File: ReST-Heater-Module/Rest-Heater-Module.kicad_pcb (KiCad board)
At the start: 2 copper layers, 24.5 x 29.5 mm, 17 parts

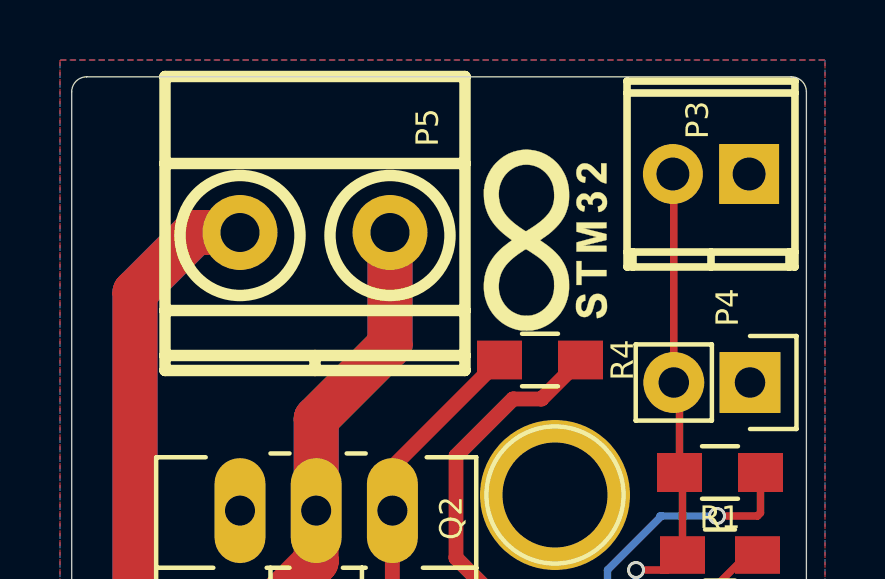
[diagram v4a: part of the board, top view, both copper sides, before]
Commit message: Added IRLML2502 Module and added Ground vias everywhere
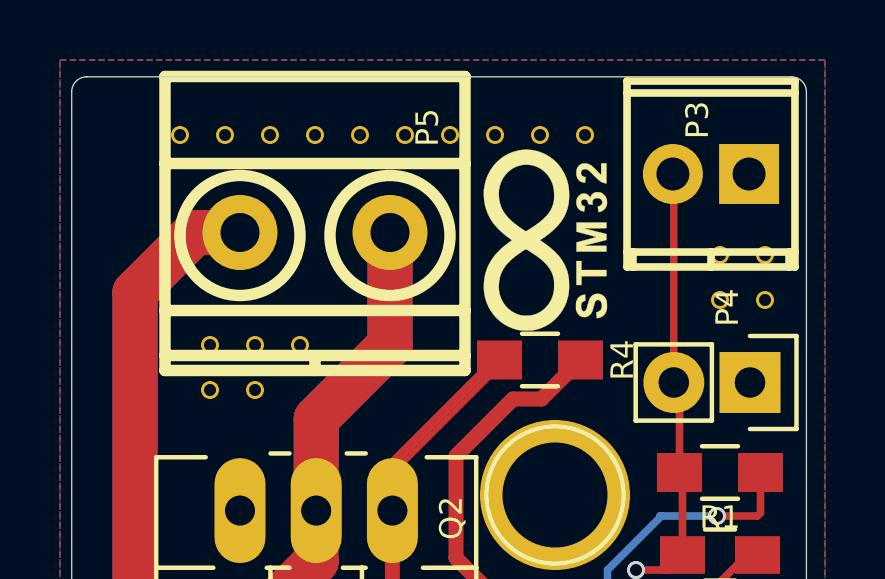
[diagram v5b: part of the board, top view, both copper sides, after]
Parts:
- added 1101: , ReST-Library:VIA-0.6mm, F.Cu at (150.0, 107.0)
- added 111: , ReST-Library:VIA-0.6mm, F.Cu at (136.5, 107.0)
- added 1111: , ReST-Library:VIA-0.6mm, F.Cu at (137.5, 114.0)
- added 111111: , ReST-Library:VIA-0.6mm, F.Cu at (154.5, 111.0)
- added 111112: , ReST-Library:VIA-0.6mm, F.Cu at (154.5, 112.5)
- added 111121: , ReST-Library:VIA-0.6mm, F.Cu at (156.0, 111.0)
- added 111122: , ReST-Library:VIA-0.6mm, F.Cu at (156.0, 112.5)
- added 1112: , ReST-Library:VIA-0.6mm, F.Cu at (137.5, 115.5)
- added 1121: , ReST-Library:VIA-0.6mm, F.Cu at (139.0, 114.0)
- added 1122: , ReST-Library:VIA-0.6mm, F.Cu at (139.0, 115.5)
- added 1131: , ReST-Library:VIA-0.6mm, F.Cu at (140.5, 114.0)
- added 121: , ReST-Library:VIA-0.6mm, F.Cu at (138.0, 107.0)
- added 131: , ReST-Library:VIA-0.6mm, F.Cu at (139.5, 107.0)
- added 141: , ReST-Library:VIA-0.6mm, F.Cu at (141.0, 107.0)
- added 151: , ReST-Library:VIA-0.6mm, F.Cu at (142.5, 107.0)
- added 161: , ReST-Library:VIA-0.6mm, F.Cu at (144.0, 107.0)
- added 171: , ReST-Library:VIA-0.6mm, F.Cu at (145.5, 107.0)
- added 181: , ReST-Library:VIA-0.6mm, F.Cu at (147.0, 107.0)
- added 191: , ReST-Library:VIA-0.6mm, F.Cu at (148.5, 107.0)
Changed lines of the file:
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@@
 (kicad_pcb (version 4) (host pcbnew 4.0.1-stable)
   (general
-    (links 34)
+    (links 50)
     (no_connects 0)
-    (area 132.5 104.5 159.575 143.485001)
+    (area 132.884999 105.054999 157.385001 134.605001)
     (thickness 1.6)
     (drawings 9)
     (tracks 116)
     (zones 0)
-    (modules 17)
+    (modules 36)
     (nets 11)
   )
@@
     (mod_text_size 1 1)
     (mod_text_width 0.15)
-    (pad_size 5 5)
-    (pad_drill 3.5)
+    (pad_size 0.6 0.6)
+    (pad_drill 0.4)
     (pad_to_mask_clearance 0)
     (aux_axis_origin 0 0)
@@
     (add_net "Net-(D2-Pad2)")
     (add_net "Net-(Q1-Pad3)")
+  )
+  (module ReST-Library:VIA-0.6mm (layer F.Cu)
+    (at 156 112.5)
+    (fp_text reference 111122 (at 0 3.5) (layer F.SilkS) hide
+      (effects (font (size 1 1) (thickness 0.15)))
+    )
+    (fp_text value "" (at 0 -3) (layer F.Fab) hide
+      (effects (font (size 1 1) (thickness 0.15)))
+    )
+    (pad 1 thru_hole circle (at 0 0) (size 0.6 0.6) (drill 0.4) (layers *.Cu)
+      (net 2 GND) (zone_connect 2))
+  )
+  (module ReST-Library:VIA-0.6mm (layer F.Cu)
+    (at 154.5 112.5)
+    (fp_text reference 111112 (at 0 3.5) (layer F.SilkS) hide
+      (effects (font (size 1 1) (thickness 0.15)))
+    )
+    (fp_text value "" (at 0 -3) (layer F.Fab) hide
+      (effects (font (size 1 1) (thickness 0.15)))
+    )
+    (pad 1 thru_hole circle (at 0 0) (size 0.6 0.6) (drill 0.4) (layers *.Cu)
+      (net 2 GND) (zone_connect 2))
+  )
+  (module ReST-Library:VIA-0.6mm (layer F.Cu)
+    (at 156 111)
+    (fp_text reference 111121 (at 0 3.5) (layer F.SilkS) hide
+      (effects (font (size 1 1) (thickness 0.15)))
+    )
+    (fp_text value "" (at 0 -3) (layer F.Fab) hide
+      (effects (font (size 1 1) (thickness 0.15)))
+    )
+    (pad 1 thru_hole circle (at 0 0) (size 0.6 0.6) (drill 0.4) (layers *.Cu)
+      (net 2 GND) (zone_connect 2))
+  )
+  (module ReST-Library:VIA-0.6mm (layer F.Cu)
+    (at 154.5 111)
+    (fp_text reference 111111 (at 0 3.5) (layer F.SilkS) hide
+      (effects (font (size 1 1) (thickness 0.15)))
+    )
+    (fp_text value "" (at 0 -3) (layer F.Fab) hide
+      (effects (font (size 1 1) (thickness 0.15)))
+    )
+    (pad 1 thru_hole circle (at 0 0) (size 0.6 0.6) (drill 0.4) (layers *.Cu)
+      (net 2 GND) (zone_connect 2))
+  )
+  (module ReST-Library:VIA-0.6mm (layer F.Cu)
+    (at 139 115.5)
+    (fp_text reference 1122 (at 0 3.5) (layer F.SilkS) hide
+      (effects (font (size 1 1) (thickness 0.15)))
+    )
+    (fp_text value "" (at 0 -3) (layer F.Fab) hide
+      (effects (font (size 1 1) (thickness 0.15)))
+    )
+    (pad 1 thru_hole circle (at 0 0) (size 0.6 0.6) (drill 0.4) (layers *.Cu)
+      (net 2 GND) (zone_connect 2))
+  )
+  (module ReST-Library:VIA-0.6mm (layer F.Cu)
+    (at 137.5 115.5)
+    (fp_text reference 1112 (at 0 3.5) (layer F.SilkS) hide
+      (effects (font (size 1 1) (thickness 0.15)))
+    )
+    (fp_text value "" (at 0 -3) (layer F.Fab) hide
+      (effects (font (size 1 1) (thickness 0.15)))
+    )
+    (pad 1 thru_hole circle (at 0 0) (size 0.6 0.6) (drill 0.4) (layers *.Cu)
+      (net 2 GND) (zone_connect 2))
+  )
+  (module ReST-Library:VIA-0.6mm (layer F.Cu)
+    (at 140.5 114)
+    (fp_text reference 1131 (at 0 3.5) (layer F.SilkS) hide
+      (effects (font (size 1 1) (thickness 0.15)))
+    )
+    (fp_text value "" (at 0 -3) (layer F.Fab) hide
+      (effects (font (size 1 1) (thickness 0.15)))
+    )
+    (pad 1 thru_hole circle (at 0 0) (size 0.6 0.6) (drill 0.4) (layers *.Cu)
+      (net 2 GND) (zone_connect 2))
+  )
+  (module ReST-Library:VIA-0.6mm (layer F.Cu)
+    (at 139 114)
+    (fp_text reference 1121 (at 0 3.5) (layer F.SilkS) hide
+      (effects (font (size 1 1) (thickness 0.15)))
+    )
+    (fp_text value "" (at 0 -3) (layer F.Fab) hide
+      (effects (font (size 1 1) (thickness 0.15)))
+    )
+    (pad 1 thru_hole circle (at 0 0) (size 0.6 0.6) (drill 0.4) (layers *.Cu)
+      (net 2 GND) (zone_connect 2))
+  )
+  (module ReST-Library:VIA-0.6mm (layer F.Cu)
+    (at 137.5 114)
+    (fp_text reference 1111 (at 0 3.5) (layer F.SilkS) hide
+      (effects (font (size 1 1) (thickness 0.15)))
+    )
+    (fp_text value "" (at 0 -3) (layer F.Fab) hide
+      (effects (font (size 1 1) (thickness 0.15)))
+    )
+    (pad 1 thru_hole circle (at 0 0) (size 0.6 0.6) (drill 0.4) (layers *.Cu)
+      (net 2 GND) (zone_connect 2))
+  )
+  (module ReST-Library:VIA-0.6mm (layer F.Cu)
+    (at 150 107)
+    (fp_text reference 1101 (at 0 3.5) (layer F.SilkS) hide
+      (effects (font (size 1 1) (thickness 0.15)))
+    )
+    (fp_text value "" (at 0 -3) (layer F.Fab) hide
+      (effects (font (size 1 1) (thickness 0.15)))
+    )
+    (pad 1 thru_hole circle (at 0 0) (size 0.6 0.6) (drill 0.4) (layers *.Cu)
+      (net 2 GND) (zone_connect 2))
+  )
+  (module ReST-Library:VIA-0.6mm (layer F.Cu)
+    (at 148.5 107)
+    (fp_text reference 191 (at 0 3.5) (layer F.SilkS) hide
+      (effects (font (size 1 1) (thickness 0.15)))
+    )
+    (fp_text value "" (at 0 -3) (layer F.Fab) hide
+      (effects (font (size 1 1) (thickness 0.15)))
+    )
+    (pad 1 thru_hole circle (at 0 0) (size 0.6 0.6) (drill 0.4) (layers *.Cu)
+      (net 2 GND) (zone_connect 2))
+  )
+  (module ReST-Library:VIA-0.6mm (layer F.Cu)
+    (at 147 107)
+    (fp_text reference 181 (at 0 3.5) (layer F.SilkS) hide
+      (effects (font (size 1 1) (thickness 0.15)))
+    )
+    (fp_text value "" (at 0 -3) (layer F.Fab) hide
+      (effects (font (size 1 1) (thickness 0.15)))
+    )
+    (pad 1 thru_hole circle (at 0 0) (size 0.6 0.6) (drill 0.4) (layers *.Cu)
+      (net 2 GND) (zone_connect 2))
+  )
+  (module ReST-Library:VIA-0.6mm (layer F.Cu)
+    (at 145.5 107)
+    (fp_text reference 171 (at 0 3.5) (layer F.SilkS) hide
+      (effects (font (size 1 1) (thickness 0.15)))
+    )
+    (fp_text value "" (at 0 -3) (layer F.Fab) hide
+      (effects (font (size 1 1) (thickness 0.15)))
+    )
+    (pad 1 thru_hole circle (at 0 0) (size 0.6 0.6) (drill 0.4) (layers *.Cu)
+      (net 2 GND) (zone_connect 2))
+  )
+  (module ReST-Library:VIA-0.6mm (layer F.Cu)
+    (at 144 107)
+    (fp_text reference 161 (at 0 3.5) (layer F.SilkS) hide
+      (effects (font (size 1 1) (thickness 0.15)))
+    )
+    (fp_text value "" (at 0 -3) (layer F.Fab) hide
+      (effects (font (size 1 1) (thickness 0.15)))
+    )
+    (pad 1 thru_hole circle (at 0 0) (size 0.6 0.6) (drill 0.4) (layers *.Cu)
+      (net 2 GND) (zone_connect 2))
+  )
+  (module ReST-Library:VIA-0.6mm (layer F.Cu)
+    (at 142.5 107)
+    (fp_text reference 151 (at 0 3.5) (layer F.SilkS) hide
+      (effects (font (size 1 1) (thickness 0.15)))
+    )
+    (fp_text value "" (at 0 -3) (layer F.Fab) hide
+      (effects (font (size 1 1) (thickness 0.15)))
+    )
+    (pad 1 thru_hole circle (at 0 0) (size 0.6 0.6) (drill 0.4) (layers *.Cu)
+      (net 2 GND) (zone_connect 2))
+  )
+  (module ReST-Library:VIA-0.6mm (layer F.Cu)
+    (at 141 107)
+    (fp_text reference 141 (at 0 3.5) (layer F.SilkS) hide
+      (effects (font (size 1 1) (thickness 0.15)))
+    )
+    (fp_text value "" (at 0 -3) (layer F.Fab) hide
+      (effects (font (size 1 1) (thickness 0.15)))
+    )
+    (pad 1 thru_hole circle (at 0 0) (size 0.6 0.6) (drill 0.4) (layers *.Cu)
+      (net 2 GND) (zone_connect 2))
+  )
+  (module ReST-Library:VIA-0.6mm (layer F.Cu)
+    (at 139.5 107)
+    (fp_text reference 131 (at 0 3.5) (layer F.SilkS) hide
+      (effects (font (size 1 1) (thickness 0.15)))
+    )
+    (fp_text value "" (at 0 -3) (layer F.Fab) hide
+      (effects (font (size 1 1) (thickness 0.15)))
+    )
+    (pad 1 thru_hole circle (at 0 0) (size 0.6 0.6) (drill 0.4) (layers *.Cu)
+      (net 2 GND) (zone_connect 2))
+  )
+  (module ReST-Library:VIA-0.6mm (layer F.Cu)
+    (at 138 107)
+    (fp_text reference 121 (at 0 3.5) (layer F.SilkS) hide
+      (effects (font (size 1 1) (thickness 0.15)))
+    )
+    (fp_text value "" (at 0 -3) (layer F.Fab) hide
+      (effects (font (size 1 1) (thickness 0.15)))
+    )
+    (pad 1 thru_hole circle (at 0 0) (size 0.6 0.6) (drill 0.4) (layers *.Cu)
+      (net 2 GND) (zone_connect 2))
   )
   (module Capacitors_SMD:C_0805_HandSoldering (layer F.Cu)
@@
     )
   )
+  (module ReST-Library:VIA-0.6mm (layer F.Cu)
+    (at 136.5 107)
+    (fp_text reference 111 (at 0 3.5) (layer F.SilkS) hide
+      (effects (font (size 1 1) (thickness 0.15)))
+    )
+    (fp_text value "" (at 0 -3) (layer F.Fab) hide
+      (effects (font (size 1 1) (thickness 0.15)))
+    )
+    (pad 1 thru_hole circle (at 0 0) (size 0.6 0.6) (drill 0.4) (layers *.Cu)
+      (net 2 GND) (zone_connect 2))
+  )
   (gr_arc (start 133.39 134.1) (end 133.39 134.6) (angle 90) (layer Edge.Cuts) (width 0.01))

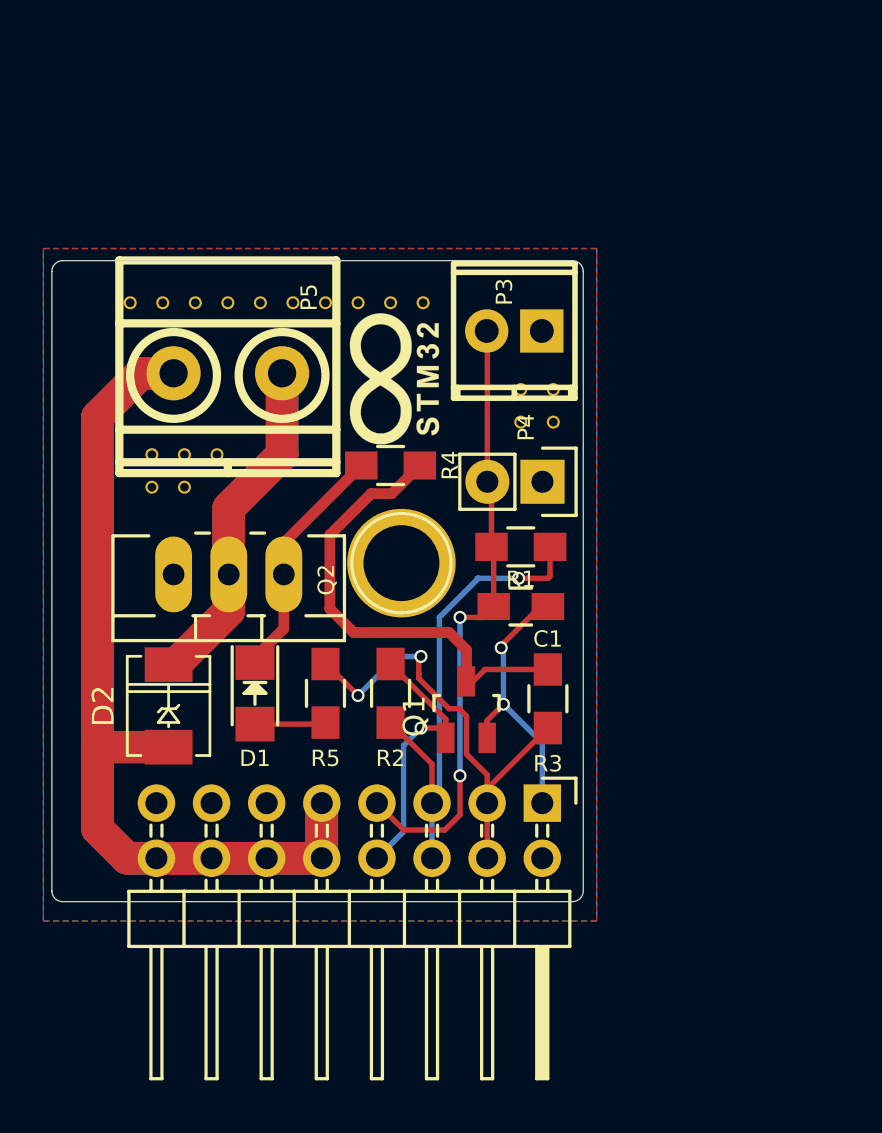
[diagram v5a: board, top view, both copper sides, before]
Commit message: Finished PCB design, notations and silkscreen
gonna work to finish a combined design for cheaper pcb cost and put
everything i need into the bom
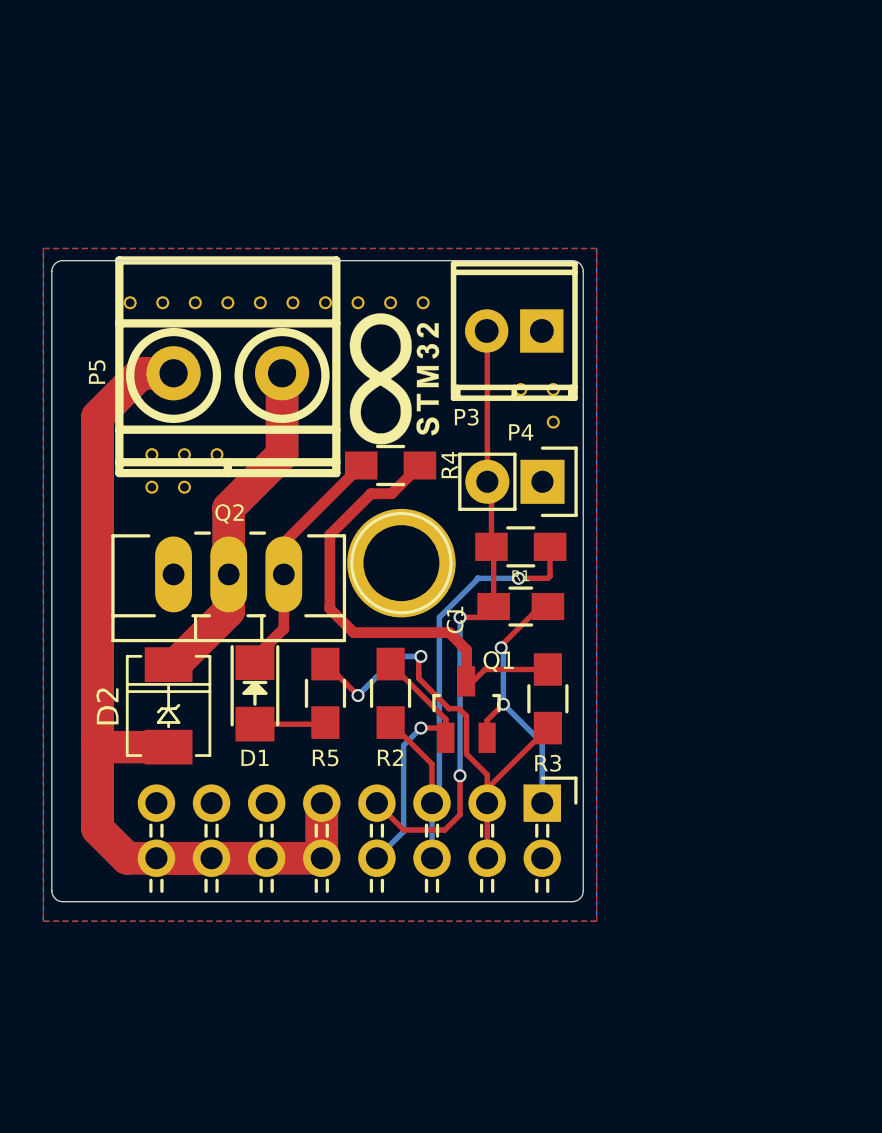
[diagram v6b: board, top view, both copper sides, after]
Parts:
- removed 111112: , ReST-Library:VIA-0.6mm
- ? (x2): renamed from G***; value LOGO -> (none)
- ?: value 1pin -> (none)
- P1: footprint Pin_Headers:Pin_Header_Angled_2x08 -> ReST-Library:Pin_Header_Angled_2x08
- moved ? 0.30 mm to (148.4, 112.7)
- renumbered 111122 to ?, 191 to ?, 181 to ?, 171 to ?, 161 to ?, 151 to ?, 141 to ?, 131 to ?, 121 to ?, 111121 to ?, 111 to ?, 111111 to ?, 1122 to ?, 1112 to ?, 1131 to ?, 1121 to ?, 1111 to ?, 1101 to ?
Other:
- board text added: "ReST32 Heater Rev. A | Test @maker_berry"
- board text removed: "ReST32 Heater Rev. A | Test PCB by Straw"

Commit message: Final release
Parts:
- moved P5 0.30 mm to (141.0, 110.5)
- moved P3 0.08 mm to (154.2, 108.4)
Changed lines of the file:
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@@
     (links 52)
     (no_connects 0)
-    (area 132.5 102.875 159.575 143.485001)
+    (area 132.5 102.875 159.575 135.500001)
     (thickness 1.6)
     (drawings 9)
@@
     (visible_elements 7FFFFFFF)
     (pcbplotparams
-      (layerselection 0x00030_80000001)
-      (usegerberextensions false)
+      (layerselection 0x010f0_80000001)
+      (usegerberextensions true)
       (excludeedgelayer true)
       (linewidth 0.100000)
@@
       (psa4output false)
       (plotreference true)
-      (plotvalue true)
+      (plotvalue false)
       (plotinvisibletext false)
       (padsonsilk false)
@@
       (outputformat 1)
       (mirror false)
-      (drillshape 1)
+      (drillshape 0)
       (scaleselection 1)
-      (outputdirectory ""))
+      (outputdirectory ../Gerber/Heater/))
   )
   (net 0 "")
@@
   )
   (module ReST-Library:screw-2,54-2P (layer F.Cu)
-    (at 154.2 108.3)
+    (at 154.175 108.375)
     (descr "2-way 2.54mm pitch terminal block, Phoenix MPT series")
     (fp_text reference P3 (at -2.2 4 180) (layer F.SilkS)
@@
   )
   (module ReST-Library:screw-5-2P (layer F.Cu)
-    (at 141 110.25)
+    (at 141 110.55)
     (descr "2-way 5mm pitch terminal block, Phoenix MKDS series")
     (fp_text reference P5 (at -6 -0.05 90) (layer F.SilkS)
